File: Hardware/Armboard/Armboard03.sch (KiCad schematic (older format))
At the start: 8 parts

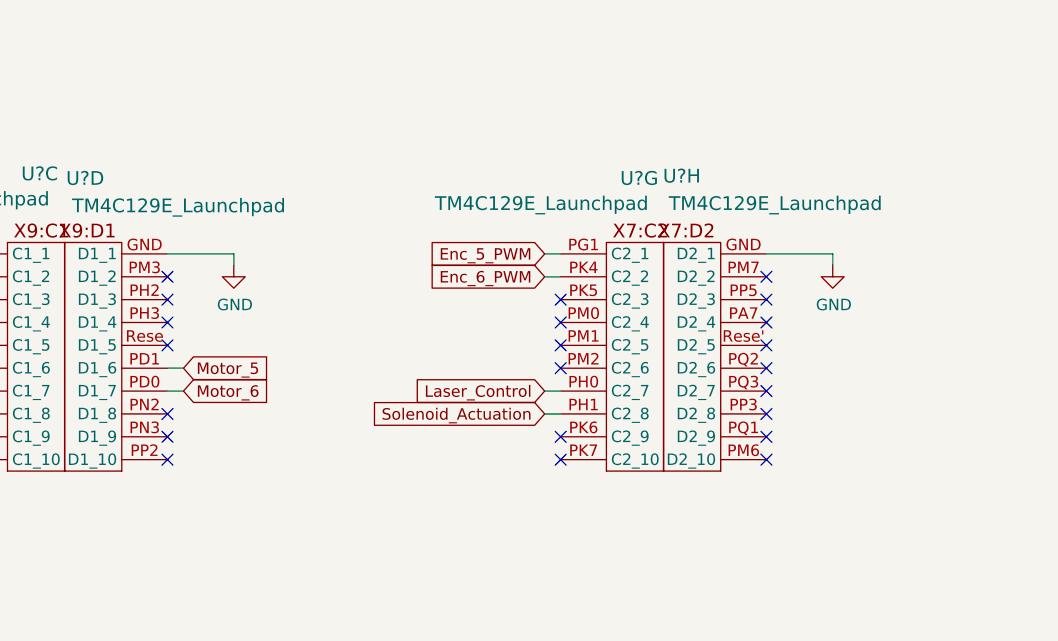
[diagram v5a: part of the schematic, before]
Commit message: Added TIVA pins to H-Bridge
Added the missing TIVA pins to the H-Bridge
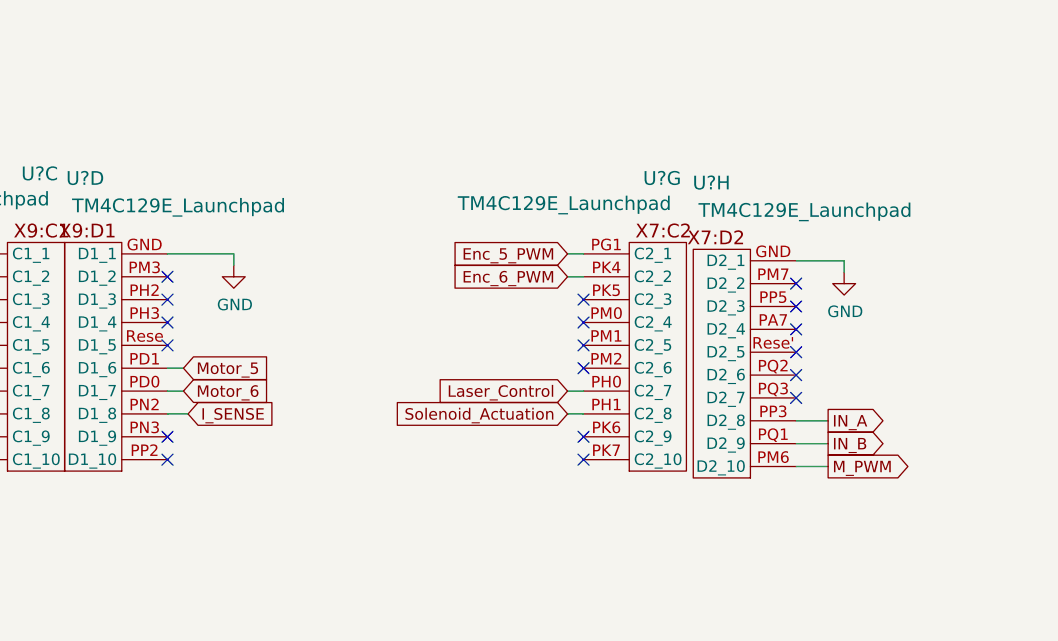
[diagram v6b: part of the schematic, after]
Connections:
- net I_SENSE: now reaches U?.PN2 (D1_8)
- net M_PWM: now reaches U?.PM6 (D2_10)
- net IN_A: now reaches U?.PP3 (D2_8)
- net IN_B: now reaches U?.PQ1 (D2_9)
- no-connect marks 50 -> 46
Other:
- moved on the sheet: U?G, U?H
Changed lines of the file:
@@
 L Armboard-rescue:TM4C129E_Launchpad-MRDT_Shields-Armboard-rescue U?
 U 7 1 5F757FE4
-P 6420 5520
-F 0 "U?" H 6480 6800 60  0000 L CNN
-F 1 "TM4C129E_Launchpad" H 5670 6690 60  0000 L CNN
-F 2 "" H 6420 5520 60  0001 C CNN
-F 3 "" H 6420 5520 60  0001 C CNN
-	7    6420 5520
+P 6520 5520
+F 0 "U?" H 6580 6800 60  0000 L CNN
+F 1 "TM4C129E_Launchpad" H 5770 6690 60  0000 L CNN
+F 2 "" H 6520 5520 60  0001 C CNN
+F 3 "" H 6520 5520 60  0001 C CNN
+	7    6520 5520
 	1    0    0    -1
 $EndComp
@@
 L Armboard-rescue:TM4C129E_Launchpad-MRDT_Shields-Armboard-rescue U?
 U 8 1 5F7598C0
-P 6920 5520
-F 0 "U?" H 7090 6810 60  0000 C CNN
-F 1 "TM4C129E_Launchpad" H 6680 6690 60  0000 C CNN
-F 2 "" H 6920 5520 60  0001 C CNN
-F 3 "" H 6920 5520 60  0001 C CNN
-	8    6920 5520
+P 7050 5550
+F 0 "U?" H 7220 6840 60  0000 C CNN
+F 1 "TM4C129E_Launchpad" H 6810 6720 60  0000 C CNN
+F 2 "" H 7050 5550 60  0001 C CNN
+F 3 "" H 7050 5550 60  0001 C CNN
+	8    7050 5550
 	-1   0    0    -1
 $EndComp
@@
 L power:GND #PWR?
 U 1 1 5F8401EF
-P 7410 4620
-F 0 "#PWR?" H 7410 4370 50  0001 C CNN
-F 1 "GND" H 7415 4447 50  0000 C CNN
-F 2 "" H 7410 4620 50  0001 C CNN
-F 3 "" H 7410 4620 50  0001 C CNN
-	1    7410 4620
-	1    0    0    -1
-$EndComp
-Wire Wire Line
-	7410 4570 7410 4620
-Wire Wire Line
-	7120 4570 7410 4570
+P 7460 4650
+F 0 "#PWR?" H 7460 4400 50  0001 C CNN
+F 1 "GND" H 7465 4477 50  0000 C CNN
+F 2 "" H 7460 4650 50  0001 C CNN
+F 3 "" H 7460 4650 50  0001 C CNN
+	1    7460 4650
+	1    0    0    -1
+$EndComp
+Wire Wire Line
+	7460 4600 7460 4650
 Text GLabel 3530 4570 0    50   Input ~ 0
 Enc_1_PWM
@@
 Wire Wire Line
 	3600 4870 3530 4870
-Text GLabel 6150 4570 0    50   Input ~ 0
+Text GLabel 6250 4570 0    50   Input ~ 0
 Enc_5_PWM
 Wire Wire Line
-	6220 4570 6150 4570
-Text GLabel 6150 4670 0    50   Input ~ 0
+	6320 4570 6250 4570
+Text GLabel 6250 4670 0    50   Input ~ 0
 Enc_6_PWM
 Wire Wire Line
-	6220 4670 6150 4670
+	6320 4670 6250 4670
 Text GLabel 7170 3340 2    50   Input ~ 0
 LS_2
@@
 Wire Wire Line
 	3610 3350 3540 3350
-Text GLabel 6150 5170 0    50   Input ~ 0
+Text GLabel 6250 5170 0    50   Input ~ 0
 Laser_Control
 Wire Wire Line
-	6220 5170 6150 5170
-Text GLabel 6150 5270 0    50   Input ~ 0
+	6320 5170 6250 5170
+Text GLabel 6250 5270 0    50   Input ~ 0
 Solenoid_Actuation
 Wire Wire Line
-	6220 5270 6150 5270
+	6320 5270 6250 5270
 Text GLabel 3540 2650 0    50   Input ~ 0
 Rx_1_Tiva
@@
 NoConn ~ 4500 4870
 NoConn ~ 4500 4970
-NoConn ~ 4500 5270
 NoConn ~ 4500 5370
 NoConn ~ 4500 5470
-NoConn ~ 6220 4770
-NoConn ~ 6220 4870
-NoConn ~ 6220 4970
-NoConn ~ 6220 5070
-NoConn ~ 6220 5370
-NoConn ~ 6220 5470
-NoConn ~ 7120 4670
-NoConn ~ 7120 4770
-NoConn ~ 7120 4870
-NoConn ~ 7120 4970
-NoConn ~ 7120 5070
-NoConn ~ 7120 5170
-NoConn ~ 7120 5270
-NoConn ~ 7120 5370
-NoConn ~ 7120 5470
+NoConn ~ 6320 4770
+NoConn ~ 6320 4870
+NoConn ~ 6320 4970
+NoConn ~ 6320 5070
+NoConn ~ 6320 5370
+NoConn ~ 6320 5470
+Wire Wire Line
+	7460 4600 7250 4600
+Wire Wire Line
+	7250 5300 7390 5300
+Wire Wire Line
+	7250 5400 7390 5400
+Text GLabel 7390 5300 2    50   Output ~ 0
+IN_A
+Text GLabel 7390 5400 2    50   Output ~ 0
+IN_B
+NoConn ~ 7250 4700
+NoConn ~ 7250 4800
+NoConn ~ 7250 4900
+NoConn ~ 7250 5000
+NoConn ~ 7250 5100
+NoConn ~ 7250 5200
+Wire Wire Line
+	7250 5500 7390 5500
+Text GLabel 7390 5500 2    50   Output ~ 0
+M_PWM
+Wire Wire Line
+	4500 5270 4590 5270
+Text GLabel 4590 5270 2    50   Input ~ 0
+I_SENSE
 $EndSCHEMATC

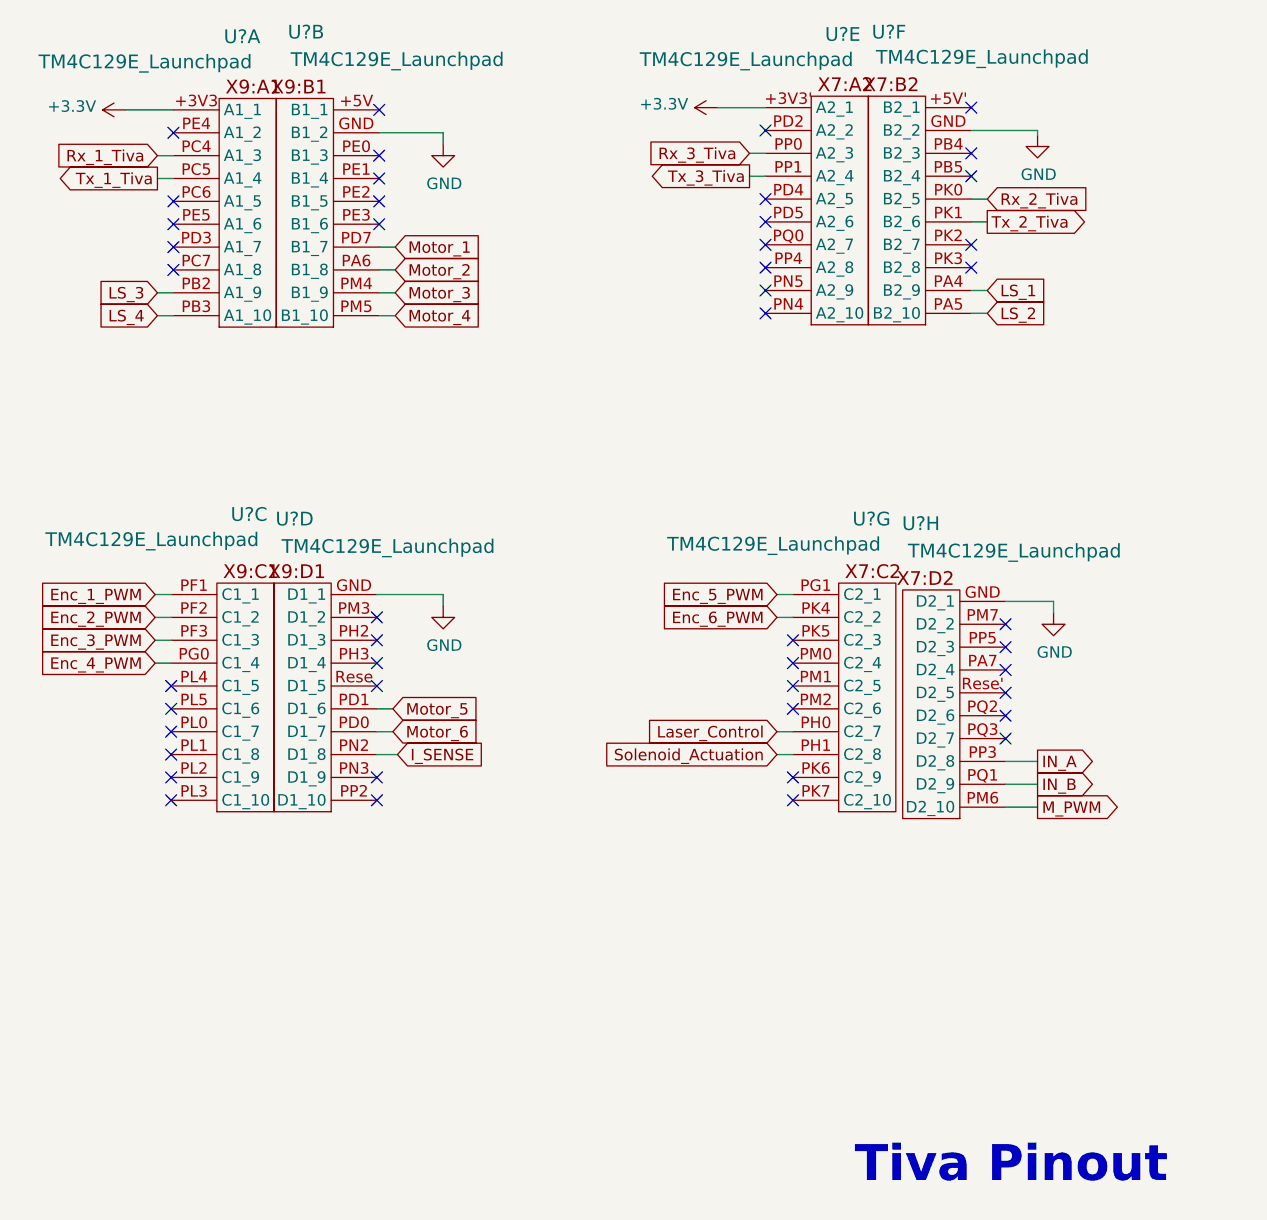
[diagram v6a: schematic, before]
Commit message: Review 2 board changes
-Connected the busses on the power and H-Bridge
-Changed the resistor value to 1.2k
-Fixed some of the pin locations on the TIVA
-Added ferrites to the H-Bridge
-Connected the buses so that they all highlight correctly
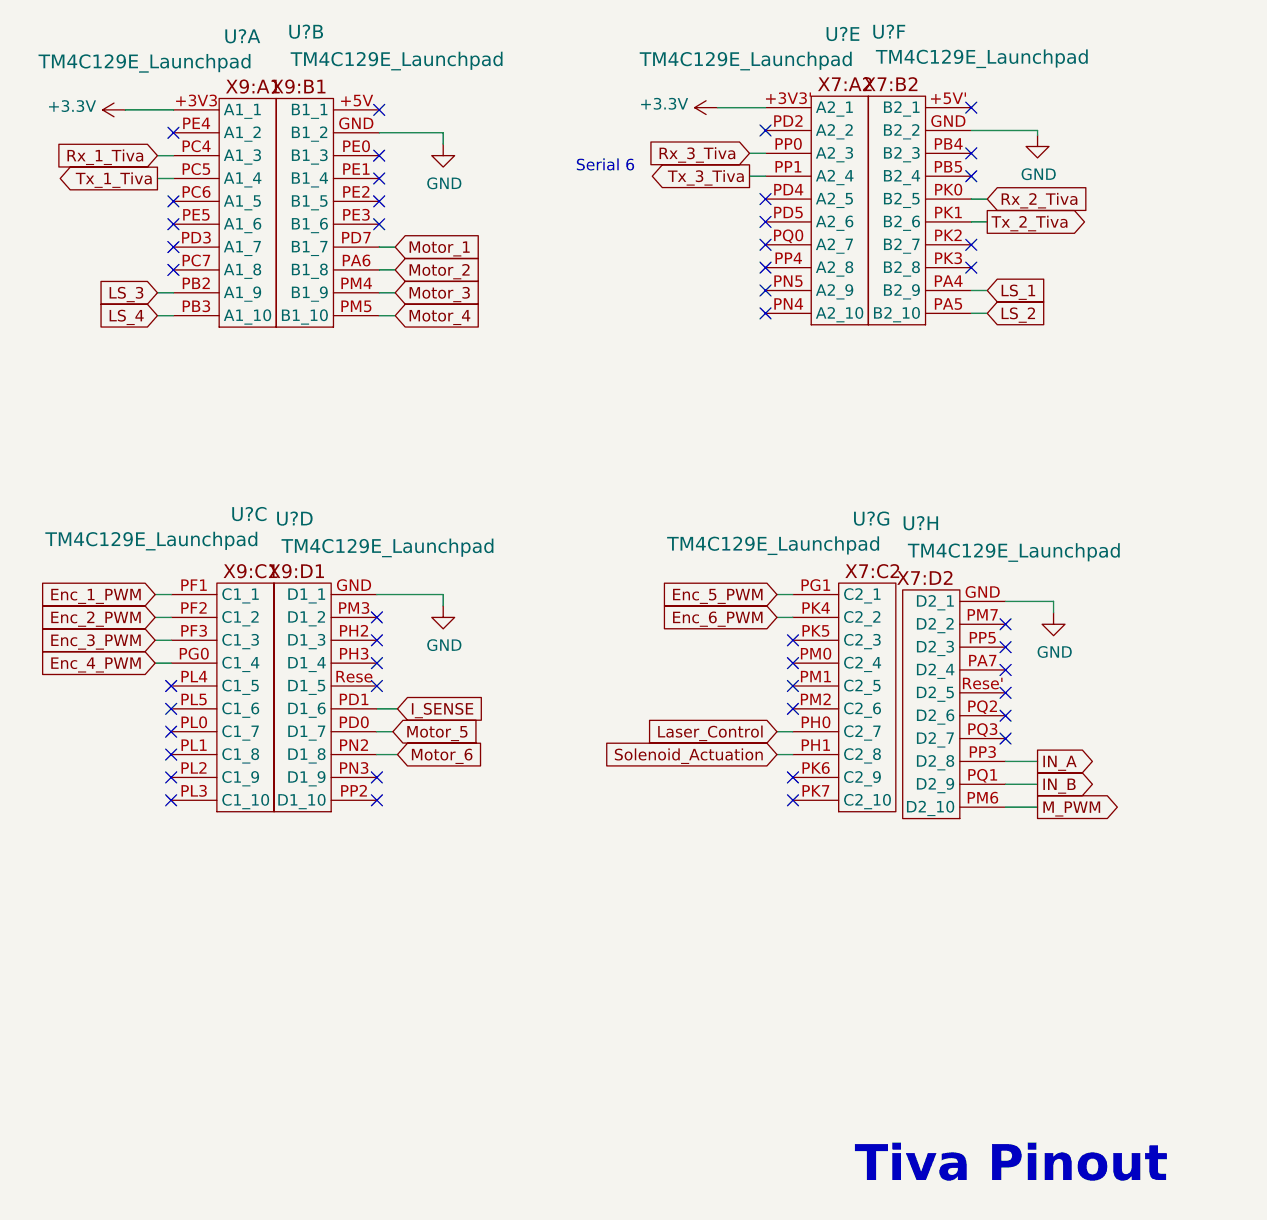
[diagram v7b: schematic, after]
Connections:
- net I_SENSE: now also U?.PD1 (D1_6); no longer U?.PN2 (D1_8)
- net Motor_5: now also U?.PD0 (D1_7); no longer U?.PD1 (D1_6)
- net Motor_6: now also U?.PN2 (D1_8); no longer U?.PD0 (D1_7)
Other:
- note added: "Serial 6"
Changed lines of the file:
@@
 $Descr A 11000 8500
 encoding utf-8
-Sheet 4 9
+Sheet 3 9
 Title ""
 Date ""
@@
 $Comp
 L Armboard-rescue:TM4C129E_Launchpad-MRDT_Shields-Armboard-rescue U?
-U 4 1 5F754D60
-P 4300 5520
-F 0 "U?" H 4460 6800 60  0000 C CNN
-F 1 "TM4C129E_Launchpad" H 4050 6680 60  0000 C CNN
-F 2 "" H 4300 5520 60  0001 C CNN
-F 3 "" H 4300 5520 60  0001 C CNN
-	4    4300 5520
-	-1   0    0    -1
-$EndComp
-$Comp
-L Armboard-rescue:TM4C129E_Launchpad-MRDT_Shields-Armboard-rescue U?
 U 5 1 5F755C93
 P 6400 3390
@@
 Wire Wire Line
 	4790 4570 4790 4620
-Wire Wire Line
-	4500 4570 4790 4570
 $Comp
 L power:GND #PWR?
@@
 Wire Wire Line
 	4510 3250 4580 3250
+Text GLabel 4590 5270 2    50   Input ~ 0
+Motor_6
 Text GLabel 4570 5170 2    50   Input ~ 0
-Motor_6
-Wire Wire Line
-	4500 5170 4570 5170
-Text GLabel 4570 5070 2    50   Input ~ 0
 Motor_5
-Wire Wire Line
-	4500 5070 4570 5070
 Text Notes 6590 7160 0    157  ~ 31
 Tiva Pinout
@@
 Text GLabel 7390 5500 2    50   Output ~ 0
 M_PWM
+Text GLabel 4590 5070 2    50   Input ~ 0
+I_SENSE
 Wire Wire Line
 	4500 5270 4590 5270
-Text GLabel 4590 5270 2    50   Input ~ 0
-I_SENSE
+Wire Wire Line
+	4500 5170 4570 5170
+Wire Wire Line
+	4500 4570 4790 4570
+$Comp
+L Armboard-rescue:TM4C129E_Launchpad-MRDT_Shields-Armboard-rescue U?
+U 4 1 5F754D60
+P 4300 5520
+F 0 "U?" H 4460 6800 60  0000 C CNN
+F 1 "TM4C129E_Launchpad" H 4050 6680 60  0000 C CNN
+F 2 "" H 4300 5520 60  0001 C CNN
+F 3 "" H 4300 5520 60  0001 C CNN
+	4    4300 5520
+	-1   0    0    -1
+$EndComp
+Wire Wire Line
+	4500 5070 4590 5070
+Text Notes 5370 2730 0    50   ~ 0
+Serial 6
 $EndSCHEMATC

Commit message: Fixed changes from review 2 of circuit board
except the LED indicators
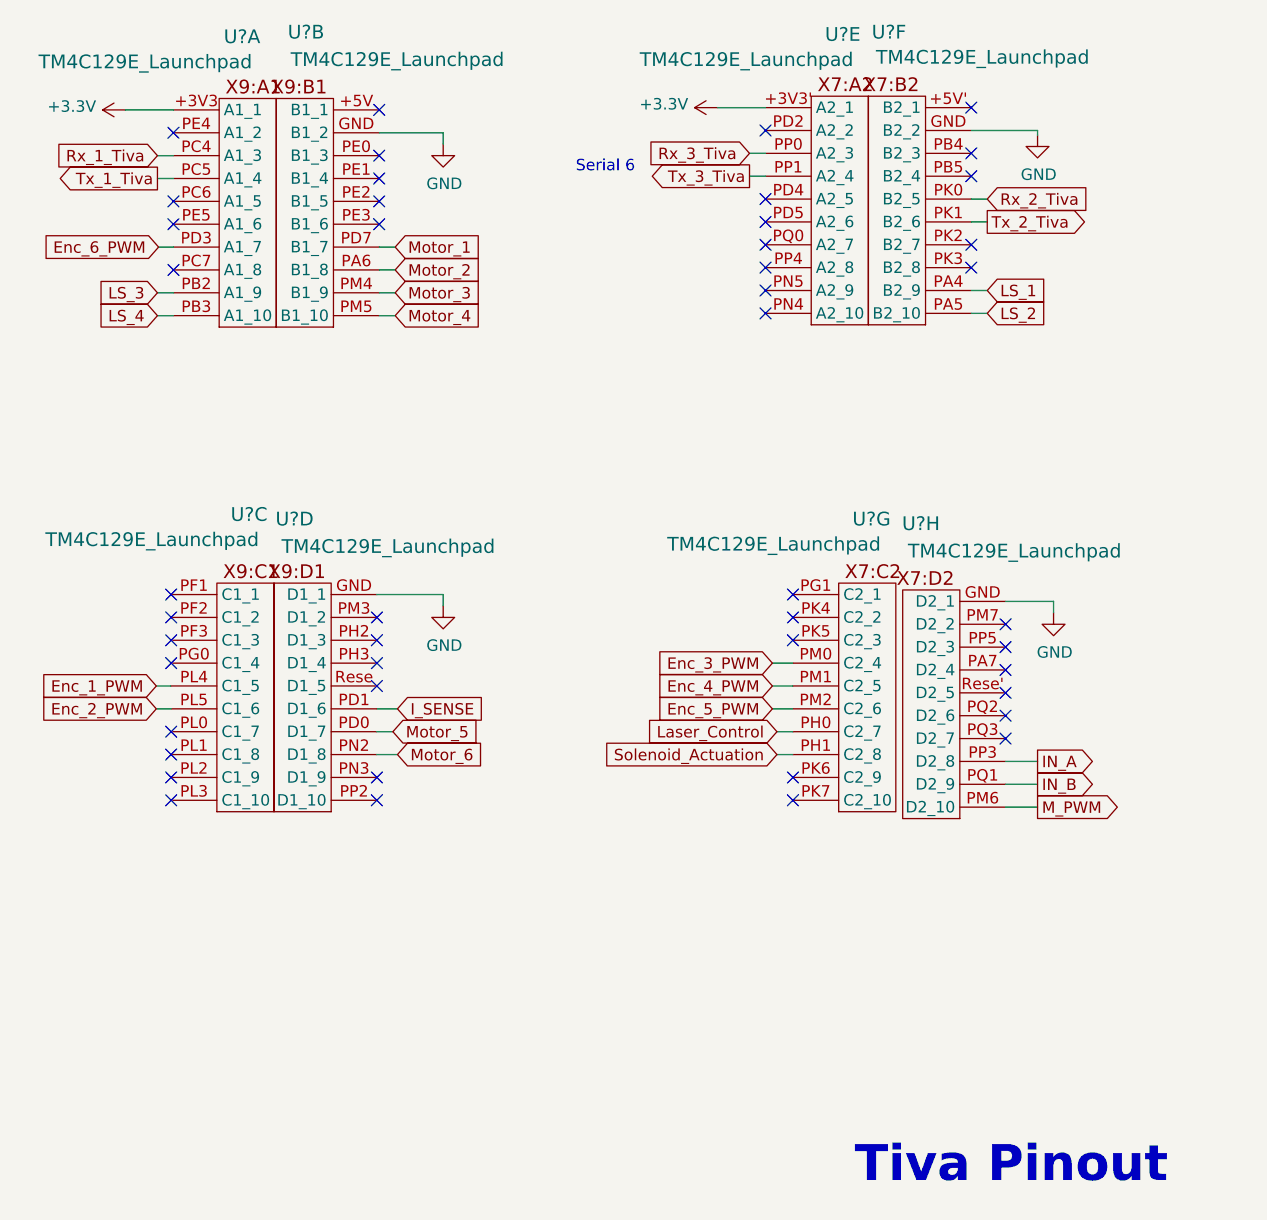
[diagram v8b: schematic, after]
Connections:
- net Enc_1_PWM: now also U?.PL4 (C1_5); no longer U?.PF1 (C1_1)
- net Enc_2_PWM: now also U?.PL5 (C1_6); no longer U?.PF2 (C1_2)
- net Enc_3_PWM: now also U?.PM0 (C2_4); no longer U?.PF3 (C1_3)
- net Enc_4_PWM: now also U?.PM1 (C2_5); no longer U?.PG0 (C1_4)
- net Enc_5_PWM: now also U?.PM2 (C2_6); no longer U?.PG1 (C2_1)
- net Enc_6_PWM: now also U?.PD3 (A1_7); no longer U?.PK4 (C2_2)
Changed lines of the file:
@@
 Wire Wire Line
 	7460 4600 7460 4650
-Text GLabel 3530 4570 0    50   Input ~ 0
+Text GLabel 3535 4970 0    50   Input ~ 0
 Enc_1_PWM
-Wire Wire Line
-	3600 4570 3530 4570
-Text GLabel 3530 4670 0    50   Input ~ 0
+Text GLabel 3535 5070 0    50   Input ~ 0
 Enc_2_PWM
-Wire Wire Line
-	3600 4670 3530 4670
-Text GLabel 3530 4770 0    50   Input ~ 0
+Text GLabel 6230 4870 0    50   Input ~ 0
 Enc_3_PWM
-Wire Wire Line
-	3600 4770 3530 4770
-Text GLabel 3530 4870 0    50   Input ~ 0
+Text GLabel 6230 4970 0    50   Input ~ 0
 Enc_4_PWM
-Wire Wire Line
-	3600 4870 3530 4870
-Text GLabel 6250 4570 0    50   Input ~ 0
+Text GLabel 6230 5070 0    50   Input ~ 0
 Enc_5_PWM
-Wire Wire Line
-	6320 4570 6250 4570
-Text GLabel 6250 4670 0    50   Input ~ 0
+Text GLabel 3545 3050 0    50   Input ~ 0
 Enc_6_PWM
-Wire Wire Line
-	6320 4670 6250 4670
 Text GLabel 7170 3340 2    50   Input ~ 0
 LS_2
@@
 NoConn ~ 3610 2850
 NoConn ~ 3610 2950
-NoConn ~ 3610 3050
 NoConn ~ 3610 3150
 NoConn ~ 4510 2650
@@
 NoConn ~ 7100 3040
 NoConn ~ 7100 3140
-NoConn ~ 3600 4970
-NoConn ~ 3600 5070
 NoConn ~ 3600 5170
 NoConn ~ 3600 5270
@@
 NoConn ~ 4500 5470
 NoConn ~ 6320 4770
-NoConn ~ 6320 4870
-NoConn ~ 6320 4970
-NoConn ~ 6320 5070
 NoConn ~ 6320 5370
 NoConn ~ 6320 5470
@@
 Text Notes 5370 2730 0    50   ~ 0
 Serial 6
+Wire Wire Line
+	3600 4970 3535 4970
+Wire Wire Line
+	3600 5070 3535 5070
+NoConn ~ 3600 4570
+NoConn ~ 3600 4670
+Wire Wire Line
+	6230 4870 6320 4870
+Wire Wire Line
+	6230 4970 6320 4970
+NoConn ~ 3600 4770
+NoConn ~ 3600 4870
+Wire Wire Line
+	6320 5070 6230 5070
+NoConn ~ 6320 4570
+Wire Wire Line
+	3610 3050 3545 3050
+NoConn ~ 6320 4670
 $EndSCHEMATC
